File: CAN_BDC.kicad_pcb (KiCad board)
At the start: 2 copper layers, 24 x 28.5 mm, 35 parts, among them P1 CONN_01X02, P2 CONN_01X05, P3 CONN_01X02, P4 CONN_01X02, P5 CONN_01X02, P6 CONN_01X02, P7 CONN_01X04, P8 CONN_01X01, P9 CONN_01X02, U1 PSD2CAN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

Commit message: Gerber generation
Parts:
- moved C5 1.87 mm to (143.3, 97.6), turned to 270 degrees
- moved C4 1.35 mm to (158.1, 104.4)
- moved P6 0.65 mm to (160.1, 110.3)
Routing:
- net GND: track 196.3 -> 212.1 mm
- net VPP: track 14.3 -> 12.1 mm
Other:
- board text added: "3V3"
- board text added: "CLK"
- board text added: "DIO"
- board text added: "GND"
- board text added: "RST"

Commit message: Buck-converter update.
Buck-converter update.
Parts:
- removed C5: 470p, Capacitors_SMD:C_0805
- removed C6: 330u, Capacitors_SMD:c_elec_6.3x7.7
- removed D1: 1N5819, Resistors_SMD:R_1206
- removed L1: 220uH, usb_ccb_custom:DE0704_Coil_2
- removed P8: CONN_01X01, usb_ccb_custom:smd1Conn
- removed R1: 2,2k, Resistors_SMD:R_0603
- removed R2: 0.33, Resistors_SMD:R_0603
- removed R3: 3,9k, Resistors_SMD:R_0603
- removed R6: 0, Resistors_SMD:R_0603
- P2: footprint usb_ccb_custom:swd_smd_conn5_x2 -> usb_ccb_custom:swd_smd_conn5
- P6: footprint Pin_Headers:Pin_Header_Straight_1x02_Pitch2.00mm -> usb_ccb_custom:AK300-2MIRROR
- U5: value MC33063 -> Mini-360; footprint usb_ccb_custom:SOIC-8 -> usb_ccb_custom:Mini-360
- moved f1 14.5 mm to (140.2, 109.9)
- moved f3 14.5 mm to (140.2, 109.9)
- moved U5 4.52 mm to (151.7, 107.3), turned to 90 degrees
- moved L2 3.01 mm to (149.6, 89.8), turned to 0 degrees
- moved P2 2.41 mm to (147.7, 85.7), turned to 180 degrees
- moved P6 1.79 mm to (161.1, 108.8), turned to 180 degrees
- moved C7 1.19 mm to (145.0, 85.9)
- moved R5 1.01 mm to (146.8, 109.9), turned to 0 degrees
- moved C8 0.85 mm to (149.6, 109.3)
- moved f2 0.74 mm to (139.8, 84.3)
- moved f4 0.74 mm to (139.8, 84.3)
- moved C2 0.72 mm to (147.6, 101.2)
- moved C9 0.39 mm to (150.6, 101.2)
- moved R4 0.35 mm to (148.6, 87.6)
- moved P7 0.15 mm to (157.7, 98.1)
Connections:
- L2 pad 1: Net-(C6-Pad1) -> Net-(L2-Pad1)
- P2 pad 2: Net-(P2-Pad2) -> SW_DIO
- P2 pad 3: GND -> SW_CLK
- P2 pad 4: SW_CLK -> GND
- P2 pad 5: SW_DIO -> Net-(P2-Pad5)
- P6 pad 1: GND -> VPP
- P6 pad 2: VPP -> GND
- R5 pad 1: Net-(P2-Pad2) -> Net-(P2-Pad5)
- U2 pad 5: Net-(U2-Pad5) -> (no net)
- U4 pad 4: Net-(P2-Pad2) -> Net-(P2-Pad5)
- U4 pad 6: Net-(U4-Pad6) -> (no net)
- U5 pad 1: Net-(R2-Pad1) -> VPP
- U5 pad 2: Net-(D1-Pad1) -> GND
- U5 pad 3: Net-(C5-Pad1) -> Net-(L2-Pad1)
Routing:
- net Net-(P2-Pad2): track 43.4 -> 0.00 mm
- net CAN_MOD: track 40.1 -> 0.42 mm
- net Net-(P2-Pad5): track 0.00 -> 36.0 mm
- net GND: track 212.1 -> 183.4 mm
- net Net-(C6-Pad1): track 16.7 -> 0.00 mm
- net Net-(C5-Pad1): track 11.2 -> 0.00 mm
- net Net-(R2-Pad2): track 10.7 -> 0.00 mm
- net Net-(D1-Pad1): track 9.43 -> 0.00 mm
- net Net-(R2-Pad1): track 8.94 -> 0.00 mm
- net Net-(R1-Pad1): track 5.54 -> 0.00 mm
- net Net-(L2-Pad1): track 0.00 -> 4.54 mm
- net Net-(U4-Pad1): track 2.82 -> 0.00 mm
- net DRV_MS1: track 11.9 -> 9.35 mm
- net SW_CLK: track 21.5 -> 19.3 mm
- net VPP: track 12.1 -> 10.1 mm
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
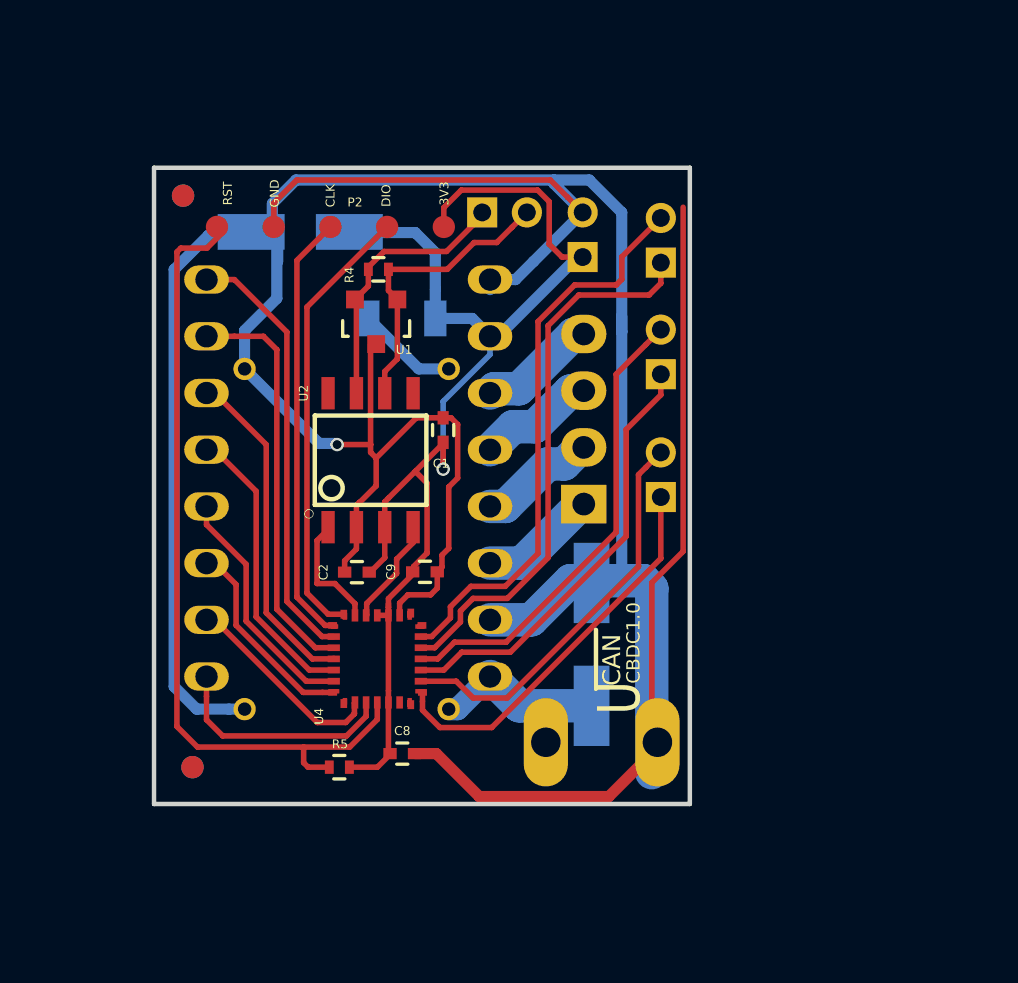
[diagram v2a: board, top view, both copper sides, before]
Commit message: Connector Footprint update
Connector Footprint update
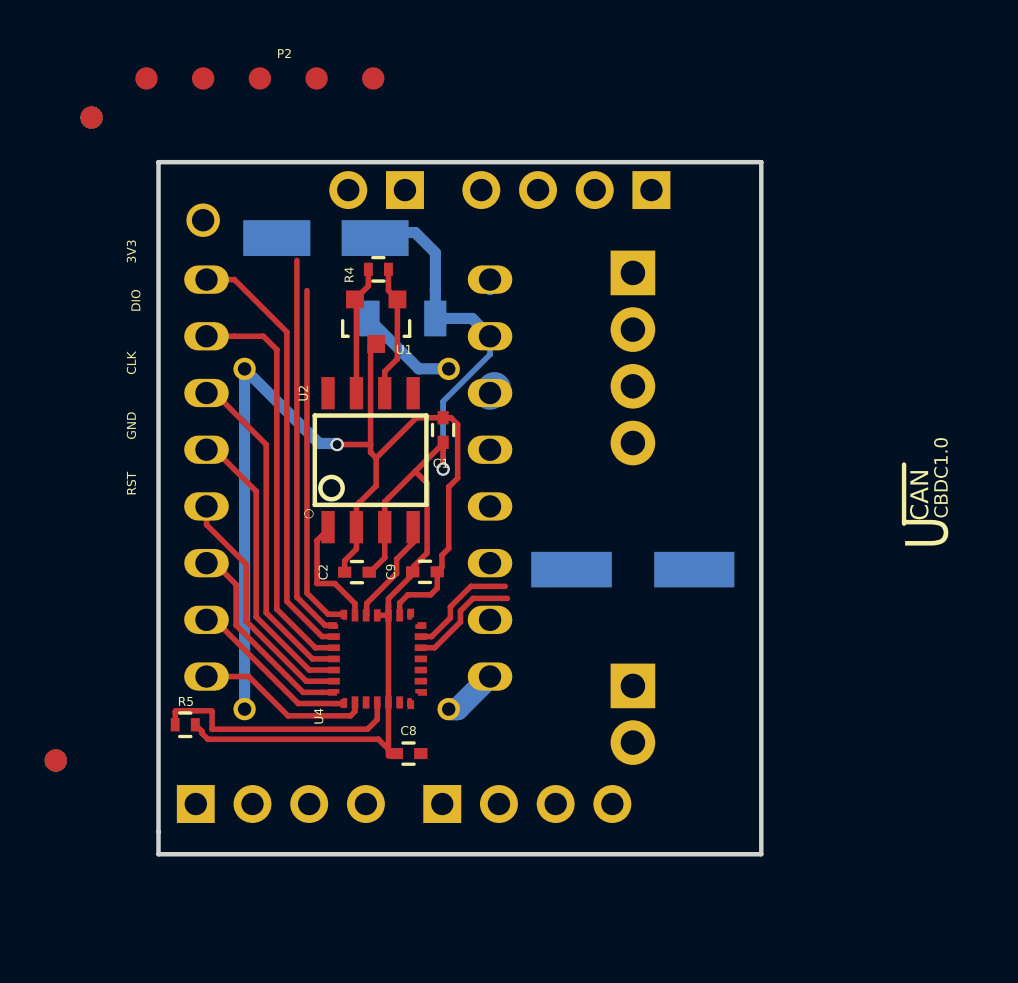
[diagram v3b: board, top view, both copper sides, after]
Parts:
- removed P3, P9: CONN_01X02, Pin_Headers:Pin_Header_Straight_1x02_Pitch2.00mm
- added BootTx1: CONN_01X01, usb_ccb_custom:1Conn, F.Cu at (140.7, 85.4)
- added P8: CONN_01X04, Pin_Headers:Pin_Header_Angled_1x04_Pitch2.54mm, B.Cu at (160.8, 84.0)
- P1: footprint Pin_Headers:Pin_Header_Straight_1x02_Pitch2.00mm -> Pin_Headers:Pin_Header_Angled_1x02_Pitch2.54mm
- P4, P5: value CONN_01X02 -> CONN_01X04; footprint Pin_Headers:Pin_Header_Straight_1x02_Pitch2.00mm -> Pin_Headers:Pin_Header_Angled_1x04_Pitch2.54mm
- P6: footprint usb_ccb_custom:AK300-2MIRROR -> Terminal_Blocks:TerminalBlock_Pheonix_MPT-2.54mm_2pol
- P7: footprint Pin_Headers:Pin_Header_Straight_1x04 -> Terminal_Blocks:TerminalBlock_Pheonix_MPT-2.54mm_4pol
- moved P4 25.0 mm to (140.4, 111.5), turned to 270 degrees
- moved P5 21.6 mm to (151.4, 111.5), turned to 270 degrees
- moved P7 10.6 mm to (159.9, 87.8), turned to 270 degrees
- moved P2 7.36 mm to (144.5, 79.0)
- moved R5 7.16 mm to (139.9, 108.0)
- moved f1 6.13 mm to (134.1, 109.6)
- moved f3 6.13 mm to (134.1, 109.6)
- moved f2 5.39 mm to (135.7, 80.8)
- moved f4 5.39 mm to (135.7, 80.8)
- moved C4 3.83 mm to (159.9, 101.0), turned to 0 degrees
- moved P1 3.60 mm to (149.7, 84.0), turned to 90 degrees
- moved P6 2.75 mm to (159.9, 106.3), turned to 270 degrees
- moved C7 1.18 mm to (146.2, 86.2)
- moved C8 0.28 mm to (149.9, 109.3)
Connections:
- P4 pad 1: /USART_TX -> /USART_RX
- P4 pad 2: /USART_RX -> /USART_TX
- P5 pad 1: /GPIO1 -> /GPIO2
- P5 pad 2: /GPIO2 -> /GPIO1
- R4 pad 1: Net-(P1-Pad1) -> Net-(P1-Pad2)
- R4 pad 2: Net-(P1-Pad2) -> Net-(P1-Pad1)
- U1 pad 1: Net-(P1-Pad2) -> Net-(P1-Pad1)
- U1 pad 2: Net-(P1-Pad1) -> Net-(P1-Pad2)
- U2 pad 5: (no net) -> Net-(U2-Pad5)
- U2 pad 6: Net-(P1-Pad2) -> Net-(P1-Pad1)
- U2 pad 7: Net-(P1-Pad1) -> Net-(P1-Pad2)
- U3 pad 11: Net-(P7-Pad4) -> Net-(P7-Pad1)
- U3 pad 12: Net-(P7-Pad3) -> Net-(P7-Pad2)
- U3 pad 13: Net-(P7-Pad2) -> Net-(P7-Pad3)
- U3 pad 14: Net-(P7-Pad1) -> Net-(P7-Pad4)
- U4 pad 1: Net-(U4-Pad1) -> DRV_MS1
- U4 pad 2: DRV_MS1 -> DRV_nENABLE
- U4 pad 3: DRV_nENABLE -> Net-(U4-Pad3)
- U4 pad 6: (no net) -> Net-(U4-Pad6)
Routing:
- net GND: track 183.4 -> 49.7 mm
- net Net-(P2-Pad5): track 36.0 -> 11.4 mm
- net /GPIO2: track 21.0 -> 0.00 mm
- net /GPIO4: track 25.5 -> 5.00 mm
- net /GPIO3: track 24.8 -> 5.08 mm
- net /GPIO1: track 19.6 -> 0.00 mm
- net /USART_RX: track 18.0 -> 0.00 mm
- net /USART_TX: track 17.7 -> 0.00 mm
- net (no net): track 0.00 -> 15.2 mm
- net VPP: track 10.1 -> 2.45 mm
- net +3V3: track 56.7 -> 49.4 mm
- net Net-(P1-Pad2): track 13.2 -> 5.99 mm
- net Net-(P1-Pad1): track 12.6 -> 5.95 mm
- net Net-(P7-Pad4): track 5.14 -> 0.00 mm
- net Net-(P7-Pad2): track 5.14 -> 0.00 mm
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- removed copper zone on B.Cu, net GND
- removed copper zone on F.Cu, net GND
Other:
- board size 24 x 28.5 mm -> 27 x 31 mm

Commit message: Layout update
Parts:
- removed BootTx1: CONN_01X01, usb_ccb_custom:1Conn
- added P3: CONN_01X02, Pin_Headers:Pin_Header_Straight_1x02_Pitch2.54mm, B.Cu at (141.4, 81.3)
- added P9: CONN_01X02, Pin_Headers:Pin_Header_Straight_1x02_Pitch2.54mm, B.Cu at (150.2, 84.0)
- C4: footprint Capacitors_SMD:c_elec_6.3x7.7 -> Capacitors_SMD:c_elec_6.3x5.3
- P1: footprint Pin_Headers:Pin_Header_Angled_1x02_Pitch2.54mm -> Pin_Headers:Pin_Header_Straight_1x02_Pitch2.54mm
- P4, P5, P8: footprint Pin_Headers:Pin_Header_Angled_1x04_Pitch2.54mm -> Pin_Headers:Pin_Header_Straight_1x04_Pitch2.54mm
- moved P5 28.8 mm to (161.5, 84.5), turned to 90 degrees
- moved f1 20.6 mm to (154.7, 109.8)
- moved f3 20.6 mm to (154.7, 109.8)
- moved f2 8.46 mm to (143.4, 84.2)
- moved f4 8.46 mm to (143.4, 84.2)
- moved P4 7.81 mm to (148.0, 110.0), turned to 90 degrees
- moved P2 7.16 mm to (146.0, 86.0)
- moved P1 3.04 mm to (150.2, 81.0)
- moved P8 2.85 mm to (161.5, 81.3)
- moved P6 2.53 mm to (160.9, 108.6), turned to 180 degrees
- moved C7 2.10 mm to (146.2, 88.3)
- moved L2 1.89 mm to (151.2, 88.8), turned to 90 degrees
- moved C8 1.00 mm to (150.9, 109.3)
- moved C4 0.60 mm to (159.7, 101.6), turned to 90 degrees
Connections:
- P6 pad 1: VPP -> GND
- P6 pad 2: GND -> VPP
- U2 pad 5: Net-(U2-Pad5) -> (no net)
- U4 pad 1: DRV_MS1 -> Net-(U4-Pad1)
- U4 pad 2: DRV_nENABLE -> DRV_MS1
- U4 pad 3: Net-(U4-Pad3) -> DRV_nENABLE
- U4 pad 6: Net-(U4-Pad6) -> (no net)
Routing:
- net GND: track 49.7 -> 102.4 mm
- net Net-(P2-Pad5): track 11.4 -> 33.5 mm
- net +3V3: track 49.4 -> 62.4 mm
- net VPP: track 2.45 -> 14.1 mm
- net Net-(P7-Pad4): track 0.00 -> 8.63 mm
- net Net-(P7-Pad2): track 0.00 -> 8.63 mm
- net Net-(P7-Pad3): track 0.00 -> 8.63 mm
- net Net-(P7-Pad1): track 0.27 -> 8.63 mm
- net Net-(P1-Pad1): track 5.95 -> 13.2 mm
- net Net-(P1-Pad2): track 5.99 -> 13.1 mm
- net DRV_DIR: track 19.4 -> 26.4 mm
- net SW_CLK: track 17.2 -> 23.9 mm
- net SW_DIO: track 15.6 -> 18.9 mm
- net Net-(L2-Pad1): track 4.54 -> 1.97 mm
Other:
- board size 27 x 31 mm -> 25 x 31.8 mm

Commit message: layout update
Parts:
- moved P8 29.6 mm to (154.4, 110.0), turned to 270 degrees
- moved P6 27.1 mm to (159.4, 81.5), turned to 0 degrees
- moved P5 23.3 mm to (154.4, 106.8), turned to 270 degrees
- moved f2 13.0 mm to (156.4, 84.0)
- moved f4 13.0 mm to (156.4, 84.0)
- moved C4 12.3 mm to (159.4, 89.3)
- moved f1 9.57 mm to (148.4, 117.0)
- moved f3 9.55 mm to (148.2, 116.8)
- moved P7 7.46 mm to (160.2, 95.2)
- moved P9 6.45 mm to (155.9, 81.0)
- moved C8 3.08 mm to (148.2, 107.8), turned to 180 degrees
- moved C7 2.76 mm to (145.9, 85.5)
- moved L2 2.75 mm to (151.2, 86.0)
- moved U3 2.75 mm to (147.2, 94.2)
- moved U5 2.75 mm to (151.7, 104.5)
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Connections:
- P5 pad 1: /GPIO2 -> GPIO3
- P5 pad 2: /GPIO1 -> GPIO4
- P8 pad 1: /GPIO4 -> GPIO1
- P8 pad 2: /GPIO3 -> GPIO2
- U4 pad 10: /GPIO1 -> (no net)
- U4 pad 11: /GPIO2 -> (no net)
- U4 pad 12: /GPIO3 -> GPIO3
- U4 pad 13: /GPIO4 -> GPIO4
- U4 pad 6: (no net) -> GPIO1
- U4 pad 7: Net-(U4-Pad7) -> GPIO2
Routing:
- net +3V3: track 62.4 -> 91.9 mm, vias 1 -> 2
- net VPP: track 14.1 -> 38.0 mm
- net (no net): track 15.2 -> 0.00 mm
- net GPIO4: track 0.00 -> 10.2 mm
- net GPIO2: track 0.00 -> 9.40 mm
- net GPIO1: track 0.00 -> 8.03 mm
- net /USART_TX: track 0.00 -> 8.02 mm
- net GPIO3: track 0.00 -> 6.78 mm
- net /USART_RX: track 0.00 -> 5.70 mm
- net Net-(P1-Pad2): track 13.1 -> 18.7 mm
- net Net-(P1-Pad1): track 13.2 -> 18.7 mm
- net /GPIO3: track 5.08 -> 0.00 mm
- net /GPIO4: track 5.00 -> 0.00 mm
- net SW_CLK: track 23.9 -> 21.7 mm
- net DRV_nENABLE: track 7.46 -> 9.33 mm
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
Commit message: Tracks update
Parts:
- moved R5 3.08 mm to (143.4, 107.3)
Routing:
- net GND: track 102.7 -> 120.8 mm
- net /USART_RX: track 5.70 -> 10.5 mm, vias 0 -> 1
- net +3V3: track 91.9 -> 89.0 mm
- net /USART_TX: track 8.02 -> 10.9 mm, vias 0 -> 1
- net Net-(P2-Pad5): track 32.4 -> 31.7 mm
- net GPIO1: track 8.03 -> 8.68 mm
- net GPIO4: track 10.2 -> 10.7 mm
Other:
- board text added: "Dziury na sruby"

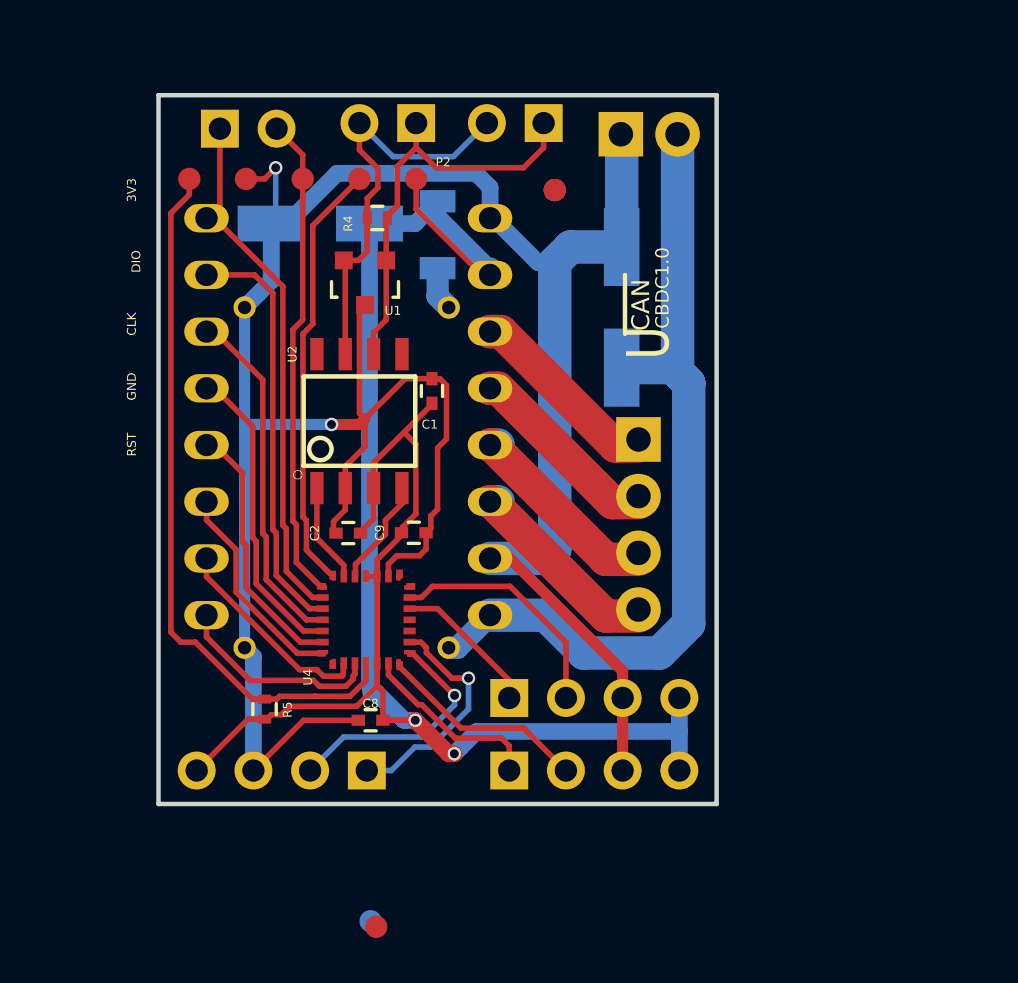
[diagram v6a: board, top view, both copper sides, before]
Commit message: DRV8825 and DRV8801 solder pads addition
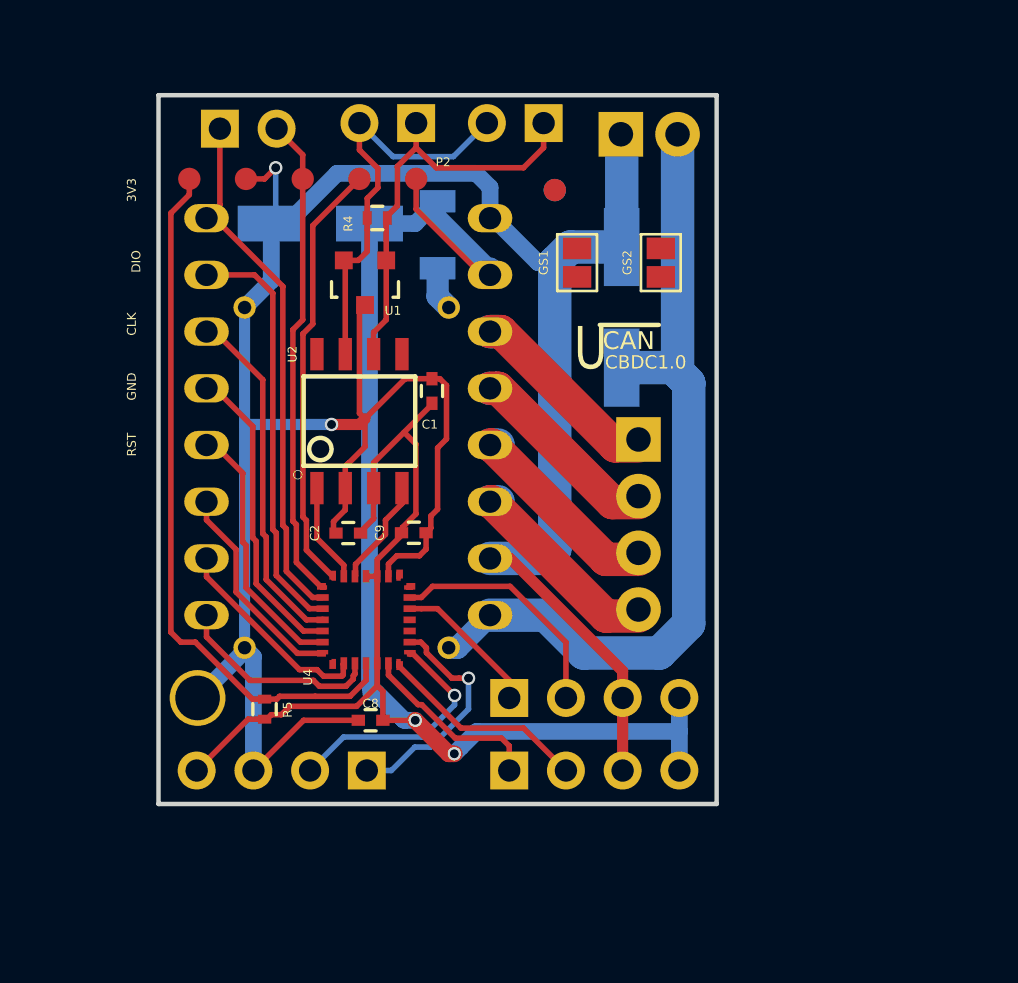
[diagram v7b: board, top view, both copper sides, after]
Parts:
- removed f3, f4: fiducial, Fiducials:Fiducial_1mm_Dia_2.54mm_Outer_CopperBottom
- added GS1: GS2, Connect:GS2, F.Cu at (157.4, 87.3)
- added GS2: GS2, Connect:GS2, F.Cu at (161.2, 87.3)
- added mh1: fiducial, usb_ccb_custom:1pin, F.Cu at (140.4, 106.8)
- U3: value POLOLU_A4988 -> POLOLU_DRV8825
- f1: moved to B.Cu
- moved f1 34.0 mm to (156.4, 84.0)
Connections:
- net Net-(P7-Pad1) renamed DRV8801_CS
- U3 pad 10: +3V3 -> DRV_nFAULT
- U4 pad 1: Net-(U4-Pad1) -> CAN_MOD
- U4 pad 15: CAN_MOD -> DRV_nFAULT
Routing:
- net DRV_nFAULT: track 0.00 -> 9.16 mm
- net +3V3: track 89.0 -> 79.9 mm
- net GND: track 120.8 -> 123.9 mm
- added copper zone on B.Cu, net GND
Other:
- board text removed: "Dziury na sruby"

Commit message: Full root
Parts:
- moved C8 0.50 mm to (148.7, 107.8)
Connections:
- mh1 pad 1: (no net) -> GND
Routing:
- net Net-(GS1-Pad1): track 0.00 -> 19.7 mm
- net CAN_MOD: track 0.42 -> 17.0 mm, vias 0 -> 2
- net Net-(GS2-Pad2): track 9.07 -> 21.4 mm
- net DRV_nFAULT: track 9.16 -> 16.8 mm, vias 0 -> 1
- net VPP: track 38.0 -> 43.4 mm
- net DRV8801_CS: track 9.14 -> 14.1 mm
- net +3V3: track 79.9 -> 81.7 mm, vias 2 -> 3
- net DRV_MS1: track 9.34 -> 9.97 mm
- added copper zone on F.Cu, net GND
